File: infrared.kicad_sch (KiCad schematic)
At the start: 3 parts, among them IC1 TSOP75338TR

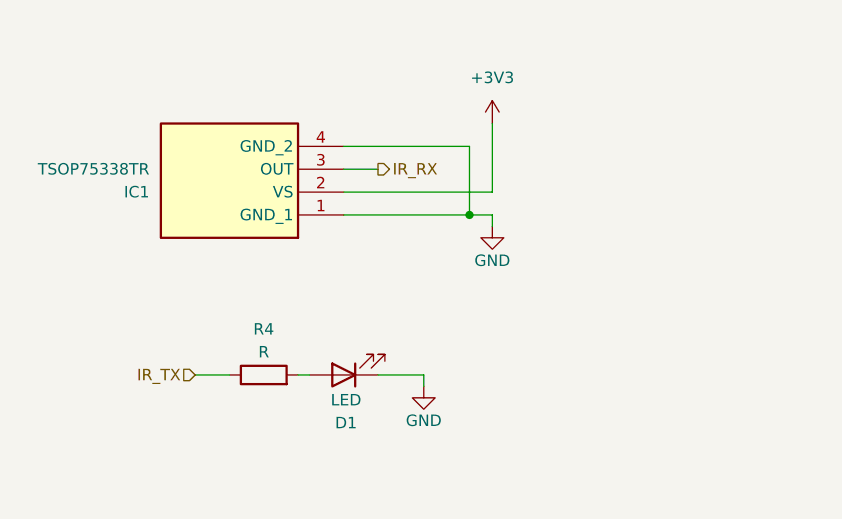
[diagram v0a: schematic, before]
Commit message: add esd usb protections
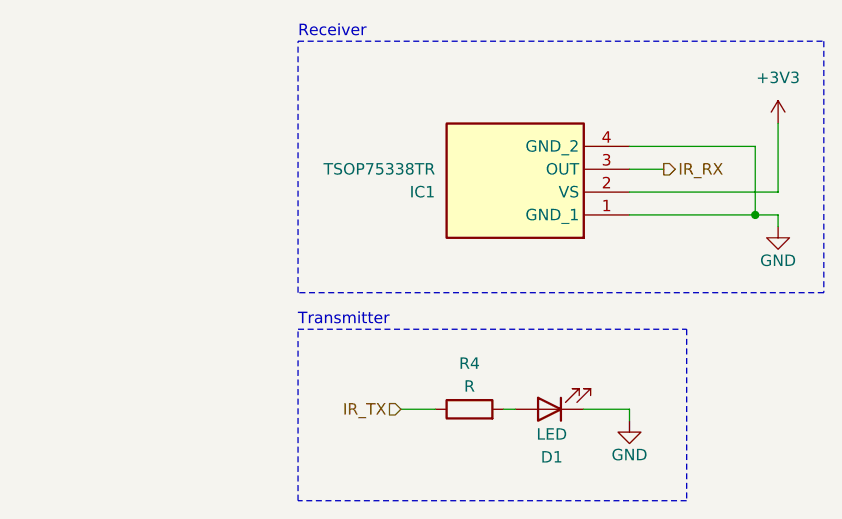
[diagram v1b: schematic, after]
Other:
- note added: "Receiver"
- note added: "Transmitter"
- moved on the sheet: D1, IC1, R4

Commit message: fix rgb led labels
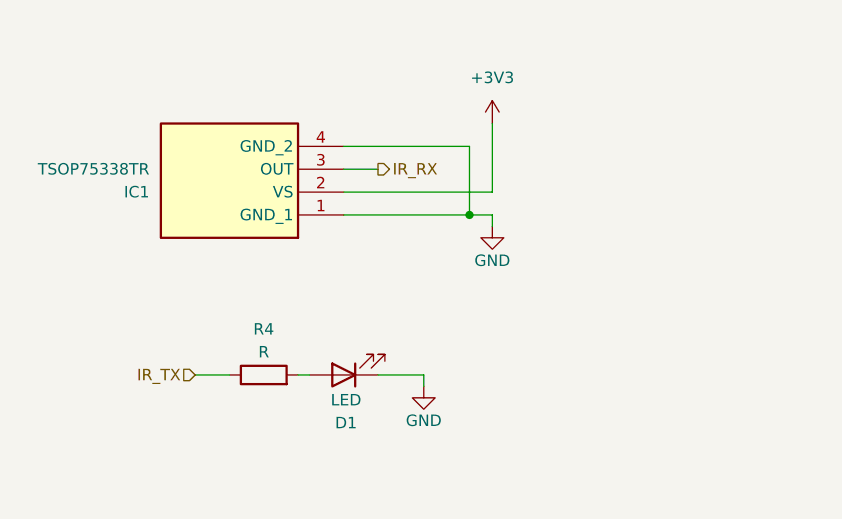
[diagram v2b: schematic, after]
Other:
- note removed: "Receiver"
- note removed: "Transmitter"
- moved on the sheet: D1, IC1, R4
